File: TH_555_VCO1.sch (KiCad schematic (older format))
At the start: 72 parts, among them J601 CV1, J602 FM_lin, J603 Sync, J604 PWM, J605 Ramp, J606 Tri, J608 555_Pulse, P601 Doepfer_Power_10pin, Q601 MMBT2222A, U601 TLC555, U602 TL074, U603 TL074

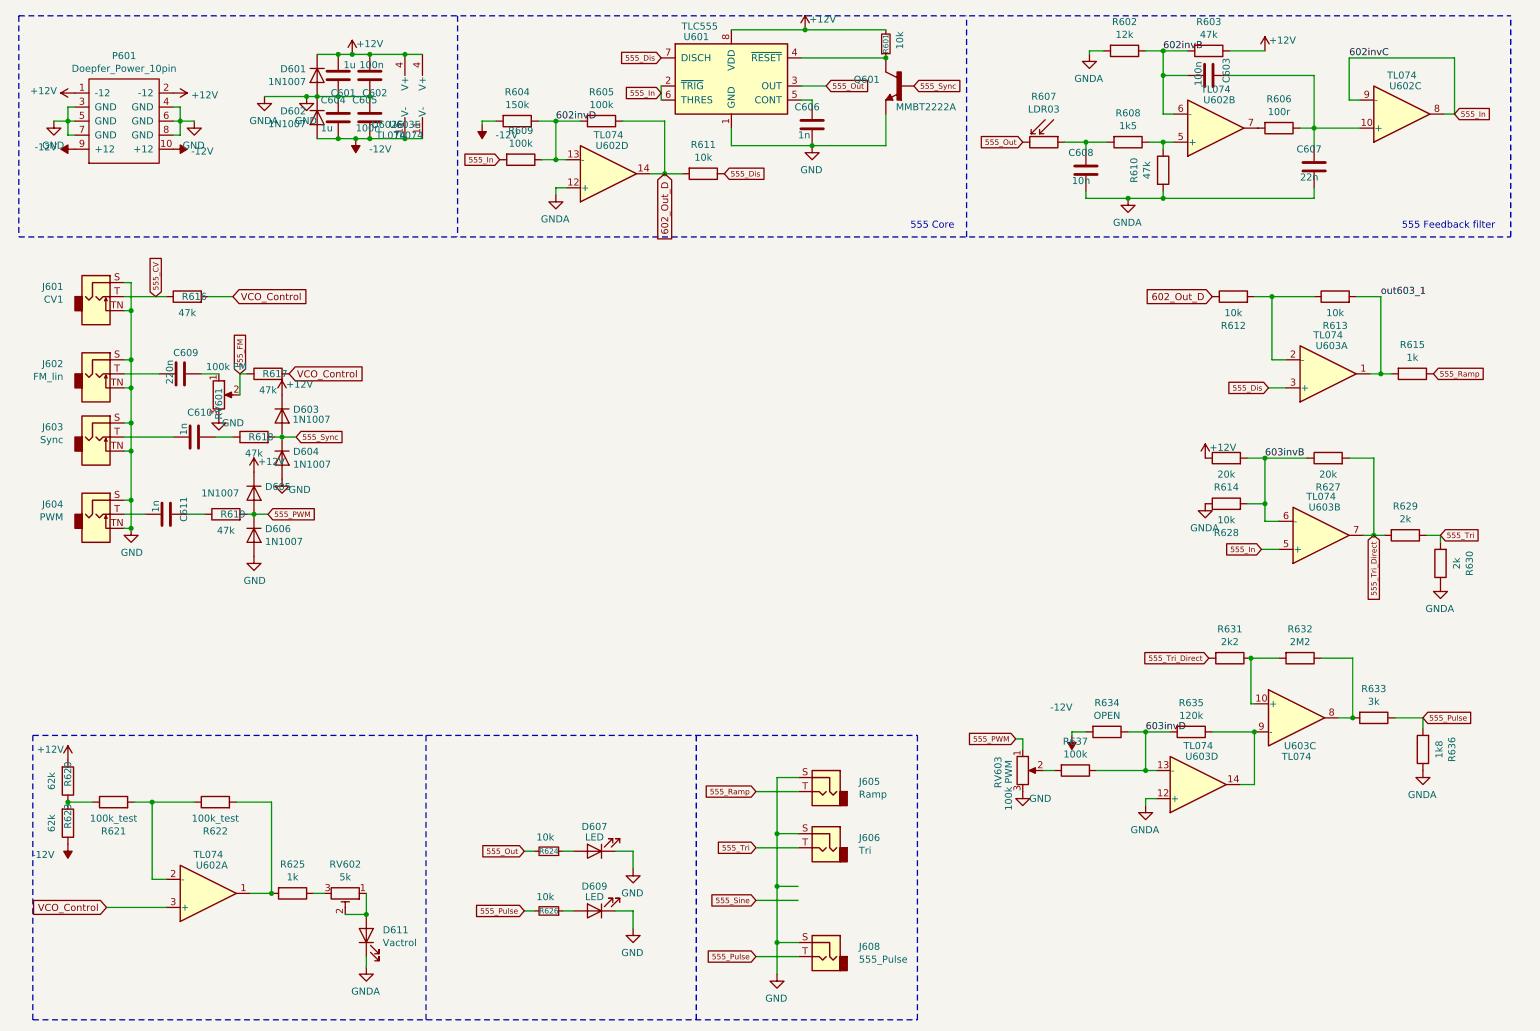
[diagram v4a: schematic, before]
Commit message: 555 sch boxes
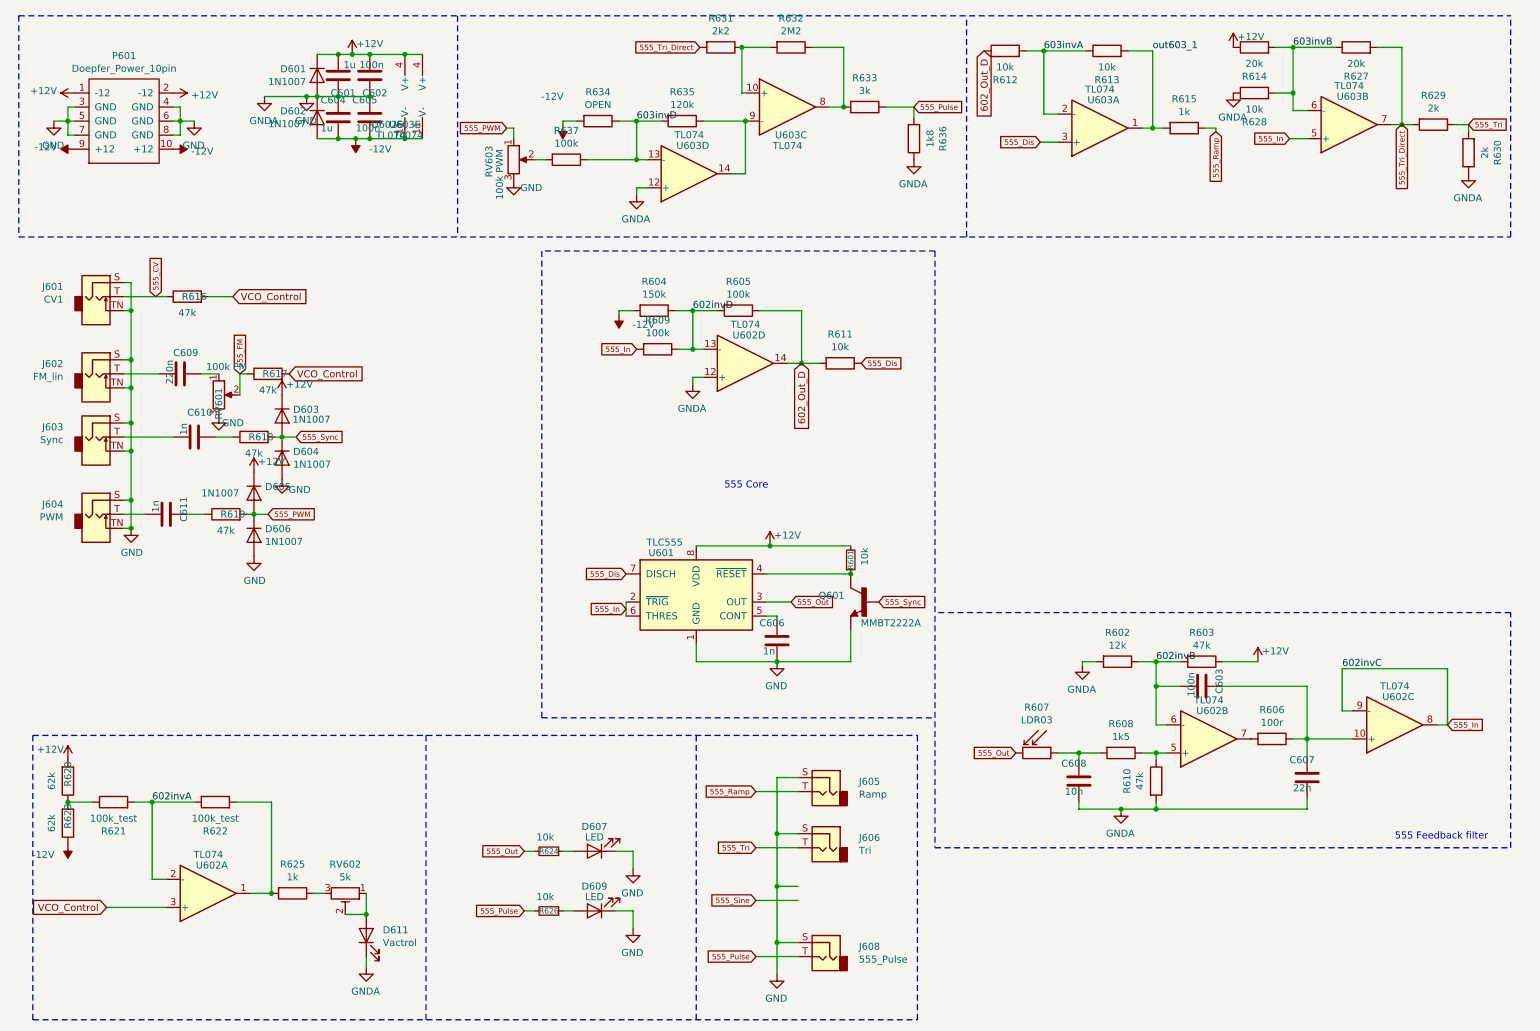
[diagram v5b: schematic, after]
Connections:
- net 602invA: now reaches R621.2, R622.1, U602.2 (-)
- net 603invA: now reaches R612.2, R613.1, U603.2 (-)
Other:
- moved on the sheet: C603, C606, C607, C608, Q601, R601, R602, R603, R604, R605, R606, R607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

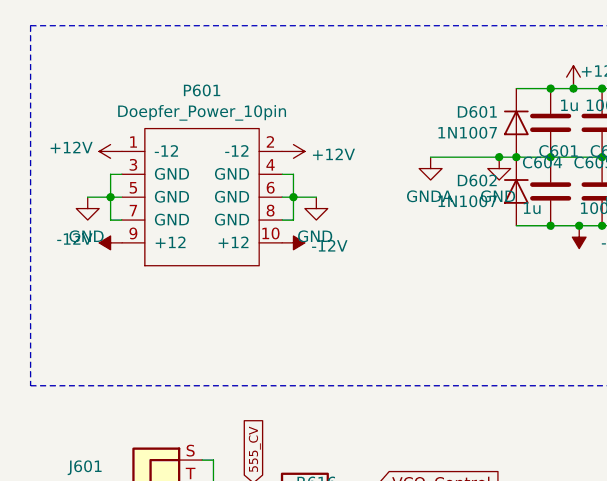
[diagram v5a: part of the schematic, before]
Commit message: Doepfer power conn reversed :o
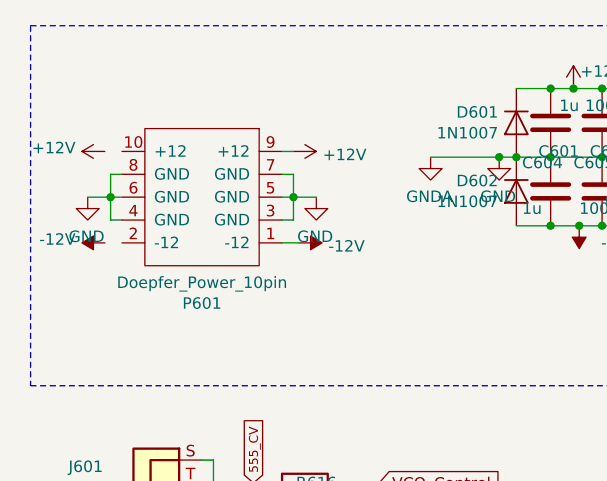
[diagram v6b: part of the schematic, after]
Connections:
- net +12V: now also P601.9 (+12); no longer P601.1 (-12), P601.2 (-12)
- net -12V: now also P601.1 (-12); no longer P601.10 (+12), P601.9 (+12)
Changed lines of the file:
@@
 L Envelope-cache-2018-08-04-13-00-04:+12V #PWR?
 U 1 1 5DD8FB32
-P 1625 1075
+P 1675 1075
 AR Path="/5DD8FB32" Ref="#PWR?"  Part="1"
 AR Path="/5CE53731/5DD8FB32" Ref="#PWR?"  Part="1"
 AR Path="/5DD87D87/5DD8FB32" Ref="#PWR0608"  Part="1"
-F 0 "#PWR0608" H 1625 925 50  0001 C CNN
-F 1 "+12V" V 1640 1203 50  0000 L CNN
-F 2 "" H 1625 1075 50  0001 C CNN
-F 3 "" H 1625 1075 50  0001 C CNN
-	1    1625 1075
+F 0 "#PWR0608" H 1675 925 50  0001 C CNN
+F 1 "+12V" V 1690 1203 50  0000 L CNN
+F 2 "" H 1675 1075 50  0001 C CNN
+F 3 "" H 1675 1075 50  0001 C CNN
+	1    1675 1075
 	0    1    1    0
 $EndComp
@@
 L power:-12V #PWR?
 U 1 1 5DD8FB3E
-P 1625 1475
+P 1700 1475
 AR Path="/5DD8FB3E" Ref="#PWR?"  Part="1"
 AR Path="/5CE53731/5DD8FB3E" Ref="#PWR?"  Part="1"
 AR Path="/5DD87D87/5DD8FB3E" Ref="#PWR0617"  Part="1"
-F 0 "#PWR0617" H 1625 1575 50  0001 C CNN
-F 1 "-12V" V 1640 1603 50  0000 L CNN
-F 2 "" H 1625 1475 50  0001 C CNN
-F 3 "" H 1625 1475 50  0001 C CNN
-	1    1625 1475
+F 0 "#PWR0617" H 1700 1575 50  0001 C CNN
+F 1 "-12V" V 1715 1603 50  0000 L CNN
+F 2 "" H 1700 1475 50  0001 C CNN
+F 3 "" H 1700 1475 50  0001 C CNN
+	1    1700 1475
 	0    1    1    0
 $EndComp
@@
 L power:-12V #PWR?
 U 1 1 5DD8FB44
-P 925 1475
+P 850 1475
 AR Path="/5DD8FB44" Ref="#PWR?"  Part="1"
 AR Path="/5CE53731/5DD8FB44" Ref="#PWR?"  Part="1"
 AR Path="/5DD87D87/5DD8FB44" Ref="#PWR0616"  Part="1"
-F 0 "#PWR0616" H 925 1575 50  0001 C CNN
-F 1 "-12V" V 940 1603 50  0000 L CNN
-F 2 "" H 925 1475 50  0001 C CNN
-F 3 "" H 925 1475 50  0001 C CNN
-	1    925  1475
+F 0 "#PWR0616" H 850 1575 50  0001 C CNN
+F 1 "-12V" V 865 1603 50  0000 L CNN
+F 2 "" H 850 1475 50  0001 C CNN
+F 3 "" H 850 1475 50  0001 C CNN
+	1    850  1475
 	0    -1   -1   0
 $EndComp
@@
 L Eurorack:Doepfer_Power_10pin P601
 U 1 1 5E362A15
-P 1275 1375
-F 0 "P601" H 1275 1940 50  0000 C CNN
-F 1 "Doepfer_Power_10pin" H 1275 1849 50  0000 C CNN
-F 2 "Connectors_IDC:IDC-Header_2x05_Pitch2.54mm_Straight" H 1275 1375 50  0001 C CNN
-F 3 "" H 1275 1375 50  0001 C CNN
-	1    1275 1375
-	1    0    0    -1
+P 1275 1175
+F 0 "P601" H 1275 1740 50  0000 C CNN
+F 1 "Doepfer_Power_10pin" H 1275 1649 50  0000 C CNN
+F 2 "Connectors_IDC:IDC-Header_2x05_Pitch2.54mm_Straight" H 1275 1175 50  0001 C CNN
+F 3 "" H 1275 1175 50  0001 C CNN
+	1    1275 1175
+	-1   0    0    1
 $EndComp
 Wire Notes Line
@@
 L Envelope-cache-2018-08-04-13-00-04:+12V #PWR?
 U 1 1 5DD8FB38
-P 925 1075
+P 850 1075
 AR Path="/5DD8FB38" Ref="#PWR?"  Part="1"
 AR Path="/5CE53731/5DD8FB38" Ref="#PWR?"  Part="1"
 AR Path="/5DD87D87/5DD8FB38" Ref="#PWR0607"  Part="1"
-F 0 "#PWR0607" H 925 925 50  0001 C CNN
-F 1 "+12V" V 940 1203 50  0000 L CNN
-F 2 "" H 925 1075 50  0001 C CNN
-F 3 "" H 925 1075 50  0001 C CNN
-	1    925  1075
+F 0 "#PWR0607" H 850 925 50  0001 C CNN
+F 1 "+12V" V 865 1203 50  0000 L CNN
+F 2 "" H 850 1075 50  0001 C CNN
+F 3 "" H 850 1075 50  0001 C CNN
+	1    850  1075
 	0    -1   -1   0
 $EndComp
@@
 Wire Notes Line
 	7050 2200 7050 6450
+Wire Wire Line
+	1625 1475 1700 1475
+Wire Wire Line
+	1675 1075 1625 1075
 $EndSCHEMATC
